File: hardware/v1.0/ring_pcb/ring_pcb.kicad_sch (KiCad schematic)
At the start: 14 parts

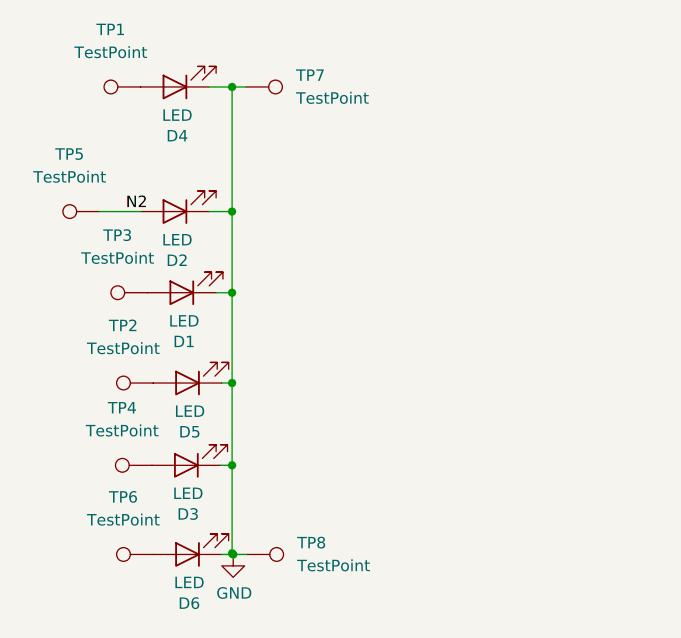
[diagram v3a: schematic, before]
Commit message: More vias and keepouts
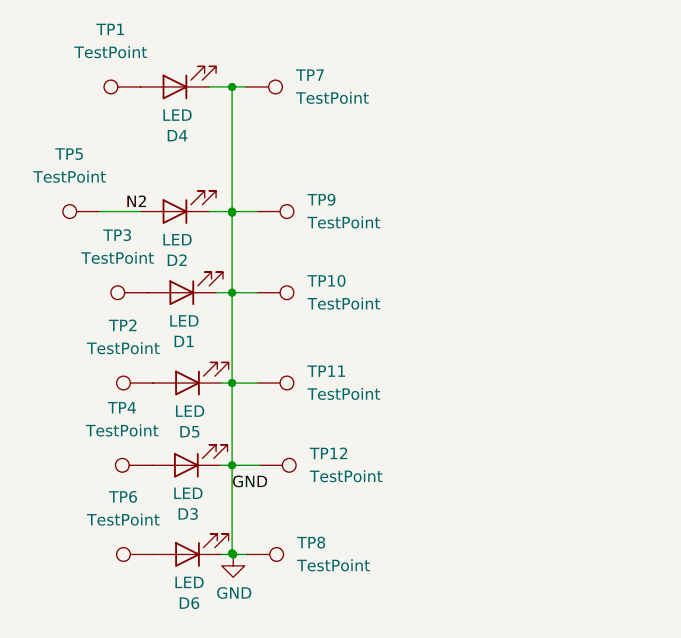
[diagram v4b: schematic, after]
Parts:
- added TP10, TP11, TP12, TP9: TestPoint, TestPoint:TestPoint_Pad_1.5x1.5mm, symbol Connector:TestPoint
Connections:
- net GND: now also D1.1 (K), D2.1 (K), D3.1 (K), D4.1 (K), D5.1 (K), TP7.1, TP10.1, TP11.1, TP12.1, TP9.1
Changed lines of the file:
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@@
 (kicad_sch (version 20210621) (generator eeschema)
   (paper "A4")
+  (junction (at 127.508 116.713) (diameter 0) (color 0 0 0 0))
+  (junction (at 127.508 87.757) (diameter 0) (color 0 0 0 0))
   (junction (at 127.508 106.934) (diameter 0) (color 0 0 0 0))
-  (junction (at 127.508 116.713) (diameter 0) (color 0 0 0 0))
-  (junction (at 127.635 116.84) (diameter 0) (color 0 0 0 0))
-  (junction (at 127.508 87.757) (diameter 0) (color 0 0 0 0))
-  (junction (at 127.508 97.79) (diameter 0) (color 0 0 0 0))
   (junction (at 127.508 78.74) (diameter 0) (color 0 0 0 0))
   (junction (at 127.508 64.897) (diameter 0) (color 0 0 0 0))
+  (junction (at 127.508 78.867) (diameter 0) (color 0 0 0 0))
+  (junction (at 127.508 97.79) (diameter 0) (color 0 0 0 0))
+  (junction (at 127.635 116.84) (diameter 0) (color 0 0 0 0))
+  (wire (pts (xy 130.302 78.74) (xy 127.508 78.74))
+    (stroke (width 0) (type default) (color 0 0 0 0))
+  )
+  (wire (pts (xy 127.508 87.757) (xy 130.302 87.757))
+    (stroke (width 0) (type default) (color 0 0 0 0))
+  )
+  (wire (pts (xy 130.556 106.934) (xy 127.508 106.934))
+    (stroke (width 0) (type default) (color 0 0 0 0))
+  )
   (wire (pts (xy 112.776 78.74) (xy 117.348 78.74))
     (stroke (width 0) (type default) (color 0 0 0 0))
   )
+  (wire (pts (xy 127.508 97.79) (xy 130.302 97.79))
+    (stroke (width 0) (type default) (color 0 0 0 0))
+  )
   (wire (pts (xy 126.365 97.79) (xy 127.508 97.79))
     (stroke (width 0) (type default) (color 0 0 0 0))
   )
+  (wire (pts (xy 127.508 78.867) (xy 127.508 78.74))
+    (stroke (width 0) (type default) (color 0 0 0 0))
+  )
+  (wire (pts (xy 127.508 64.897) (xy 127.508 64.77))
+    (stroke (width 0) (type default) (color 0 0 0 0))
+  )
+  (wire (pts (xy 127.508 78.74) (xy 127.508 64.897))
+    (stroke (width 0) (type default) (color 0 0 0 0))
+  )
+  (wire (pts (xy 127.508 87.757) (xy 127.508 78.867))
+    (stroke (width 0) (type default) (color 0 0 0 0))
+  )
   (wire (pts (xy 127.508 106.934) (xy 127.508 97.79))
     (stroke (width 0) (type default) (color 0 0 0 0))
   )
-  (wire (pts (xy 127.508 116.713) (xy 127.508 106.934))
-    (stroke (width 0) (type default) (color 0 0 0 0))
-  )
-  (wire (pts (xy 127.508 64.897) (xy 127.508 64.77))
+  (wire (pts (xy 127.508 106.934) (xy 127.508 116.713))
     (stroke (width 0) (type default) (color 0 0 0 0))
   )
@@
     (stroke (width 0) (type default) (color 0 0 0 0))
   )
-  (wire (pts (xy 127.508 78.74) (xy 127.508 64.897))
-    (stroke (width 0) (type default) (color 0 0 0 0))
-  )
-  (wire (pts (xy 127.508 87.757) (xy 127.508 78.74))
-    (stroke (width 0) (type default) (color 0 0 0 0))
-  )
   (wire (pts (xy 129.032 64.897) (xy 127.508 64.897))
     (stroke (width 0) (type default) (color 0 0 0 0))
@@
     (stroke (width 0) (type default) (color 0 0 0 0))
   )
+  (wire (pts (xy 127.635 116.84) (xy 126.365 116.84))
+    (stroke (width 0) (type default) (color 0 0 0 0))
+  )
   (wire (pts (xy 129.159 116.84) (xy 127.635 116.84))
     (stroke (width 0) (type default) (color 0 0 0 0))
   )
-  (wire (pts (xy 127.635 116.84) (xy 126.365 116.84))
-    (stroke (width 0) (type default) (color 0 0 0 0))
-  )
   (wire (pts (xy 126.238 106.934) (xy 127.508 106.934))
     (stroke (width 0) (type default) (color 0 0 0 0))
@@
   (wire (pts (xy 125.73 87.757) (xy 127.508 87.757))
     (stroke (width 0) (type default) (color 0 0 0 0))
+  )
+  (label "GND" (at 127.508 109.855 0)
+    (effects (font (size 1.27 1.27)) (justify left bottom))
   )
   (label "N2" (at 115.697 78.74 0)
@@
     (pin "2")
   )
+  (symbol (lib_id "Connector:TestPoint") (at 130.556 106.934 270) (unit 1)
+    (in_bom yes) (on_board yes) (fields_autoplaced)
+    (property "Reference" "TP12" (id 0) (at 136.144 105.6639 90)
+      (effects (font (size 1.27 1.27)) (justify left))
+    )
+    (property "Value" "TestPoint" (id 1) (at 136.144 108.2039 90)
+      (effects (font (size 1.27 1.27)) (justify left))
+    )
+    (property "Footprint" "TestPoint:TestPoint_Pad_1.5x1.5mm" (id 2) (at 130.556 112.014 0)
+      (effects (font (size 1.27 1.27)) hide)
+    )
+    (property "Datasheet" "~" (id 3) (at 130.556 112.014 0)
+      (effects (font (size 1.27 1.27)) hide)
+    )
+    (pin "1")
+  )
   (symbol (lib_id "Connector:TestPoint") (at 118.745 116.84 90) (unit 1)
     (in_bom yes) (on_board yes) (fields_autoplaced)
@@
     (pin "1")
   )
+  (symbol (lib_id "Connector:TestPoint") (at 130.302 78.74 270) (unit 1)
+    (in_bom yes) (on_board yes) (fields_autoplaced)
+    (property "Reference" "TP9" (id 0) (at 135.89 77.4699 90)
+      (effects (font (size 1.27 1.27)) (justify left))
+    )
+    (property "Value" "TestPoint" (id 1) (at 135.89 80.0099 90)
+      (effects (font (size 1.27 1.27)) (justify left))
+    )
+    (property "Footprint" "TestPoint:TestPoint_Pad_1.5x1.5mm" (id 2) (at 130.302 83.82 0)
+      (effects (font (size 1.27 1.27)) hide)
+    )
+    (property "Datasheet" "~" (id 3) (at 130.302 83.82 0)
+      (effects (font (size 1.27 1.27)) hide)
+    )
+    (pin "1")
+  )
+  (symbol (lib_id "Connector:TestPoint") (at 130.302 87.757 270) (unit 1)
+    (in_bom yes) (on_board yes) (fields_autoplaced)
+    (property "Reference" "TP10" (id 0) (at 135.89 86.4869 90)
+      (effects (font (size 1.27 1.27)) (justify left))
+    )
+    (property "Value" "TestPoint" (id 1) (at 135.89 89.0269 90)
+      (effects (font (size 1.27 1.27)) (justify left))
+    )
+    (property "Footprint" "TestPoint:TestPoint_Pad_1.5x1.5mm" (id 2) (at 130.302 92.837 0)
+      (effects (font (size 1.27 1.27)) hide)
+    )
+    (property "Datasheet" "~" (id 3) (at 130.302 92.837 0)
+      (effects (font (size 1.27 1.27)) hide)
+    )
+    (pin "1")
+  )
   (symbol (lib_id "Connector:TestPoint") (at 118.11 87.757 90) (unit 1)
     (in_bom yes) (on_board yes) (fields_autoplaced)
@@
     (pin "1")
   )
+  (symbol (lib_id "Connector:TestPoint") (at 130.302 97.79 270) (unit 1)
+    (in_bom yes) (on_board yes) (fields_autoplaced)
+    (property "Reference" "TP11" (id 0) (at 135.89 96.5199 90)
+      (effects (font (size 1.27 1.27)) (justify left))
+    )
+    (property "Value" "TestPoint" (id 1) (at 135.89 99.0599 90)
+      (effects (font (size 1.27 1.27)) (justify left))
+    )
+    (property "Footprint" "TestPoint:TestPoint_Pad_1.5x1.5mm" (id 2) (at 130.302 102.87 0)
+      (effects (font (size 1.27 1.27)) hide)
+    )
+    (property "Datasheet" "~" (id 3) (at 130.302 102.87 0)
+      (effects (font (size 1.27 1.27)) hide)
+    )
+    (pin "1")
+  )
   (symbol (lib_id "Connector:TestPoint") (at 129.159 116.84 270) (unit 1)
     (in_bom yes) (on_board yes) (fields_autoplaced)
@@
       (reference "TP8") (unit 1) (value "TestPoint") (footprint "TestPoint:TestPoint_Pad_1.5x1.5mm")
     )
-  )
+    (path "/9eb5fc74-7ee2-4483-b24f-769829d8a6c2"
+      (reference "TP9") (unit 1) (value "TestPoint") (footprint "TestPoint:TestPoint_Pad_1.5x1.5mm")
+    )
+    (path "/a72b0211-01ed-437e-8ed0-dd4a1c9ad8e3"
+      (reference "TP10") (unit 1) (value "TestPoint") (footprint "TestPoint:TestPoint_Pad_1.5x1.5mm")
+    )
+    (path "/bf1b59cd-286d-4b1f-ae75-42e14253d3af"
+      (reference "TP11") (unit 1) (value "TestPoint") (footprint "TestPoint:TestPoint_Pad_1.5x1.5mm")
+    )
+    (path "/4ef79b22-88fe-45d2-99f7-8d367793e669"
+      (reference "TP12") (unit 1) (value "TestPoint") (footprint "TestPoint:TestPoint_Pad_1.5x1.5mm")
+    )
+  )

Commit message: New PCB and Gerbers
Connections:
- net N4: now reaches D4.2 (A), TP1.1
- net N5: now reaches D5.2 (A), TP2.1
- net N3: now reaches D3.2 (A), TP4.1
- net N6: now reaches D6.2 (A), TP6.1
- net N1: now reaches D1.2 (A), TP3.1
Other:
- moved on the sheet: TP1, TP2, TP3, TP4, TP6
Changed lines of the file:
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@@
 (kicad_sch (version 20210621) (generator eeschema)
   (paper "A4")
+  (junction (at 127.508 87.757) (diameter 0) (color 0 0 0 0))
+  (junction (at 127.508 78.74) (diameter 0) (color 0 0 0 0))
   (junction (at 127.508 116.713) (diameter 0) (color 0 0 0 0))
-  (junction (at 127.508 87.757) (diameter 0) (color 0 0 0 0))
-  (junction (at 127.508 106.934) (diameter 0) (color 0 0 0 0))
-  (junction (at 127.508 78.74) (diameter 0) (color 0 0 0 0))
-  (junction (at 127.508 64.897) (diameter 0) (color 0 0 0 0))
   (junction (at 127.508 78.867) (diameter 0) (color 0 0 0 0))
   (junction (at 127.508 97.79) (diameter 0) (color 0 0 0 0))
+  (junction (at 127.508 64.897) (diameter 0) (color 0 0 0 0))
+  (junction (at 127.508 106.934) (diameter 0) (color 0 0 0 0))
   (junction (at 127.635 116.84) (diameter 0) (color 0 0 0 0))
+  (wire (pts (xy 113.792 97.79) (xy 118.745 97.79))
+    (stroke (width 0) (type default) (color 0 0 0 0))
+  )
   (wire (pts (xy 130.302 78.74) (xy 127.508 78.74))
     (stroke (width 0) (type default) (color 0 0 0 0))
@@
     (stroke (width 0) (type default) (color 0 0 0 0))
   )
+  (wire (pts (xy 114.173 116.84) (xy 118.745 116.84))
+    (stroke (width 0) (type default) (color 0 0 0 0))
+  )
   (wire (pts (xy 130.556 106.934) (xy 127.508 106.934))
     (stroke (width 0) (type default) (color 0 0 0 0))
   )
+  (wire (pts (xy 114.3 106.934) (xy 118.618 106.934))
+    (stroke (width 0) (type default) (color 0 0 0 0))
+  )
   (wire (pts (xy 112.776 78.74) (xy 117.348 78.74))
     (stroke (width 0) (type default) (color 0 0 0 0))
@@
     (stroke (width 0) (type default) (color 0 0 0 0))
   )
+  (wire (pts (xy 127.508 87.757) (xy 127.508 78.867))
+    (stroke (width 0) (type default) (color 0 0 0 0))
+  )
   (wire (pts (xy 127.508 78.867) (xy 127.508 78.74))
     (stroke (width 0) (type default) (color 0 0 0 0))
@@
     (stroke (width 0) (type default) (color 0 0 0 0))
   )
-  (wire (pts (xy 127.508 87.757) (xy 127.508 78.867))
+  (wire (pts (xy 127.508 97.79) (xy 127.508 87.757))
     (stroke (width 0) (type default) (color 0 0 0 0))
   )
@@
     (stroke (width 0) (type default) (color 0 0 0 0))
   )
-  (wire (pts (xy 127.508 97.79) (xy 127.508 87.757))
-    (stroke (width 0) (type default) (color 0 0 0 0))
-  )
   (wire (pts (xy 129.032 64.897) (xy 127.508 64.897))
     (stroke (width 0) (type default) (color 0 0 0 0))
@@
     (stroke (width 0) (type default) (color 0 0 0 0))
   )
+  (wire (pts (xy 112.776 64.897) (xy 117.348 64.897))
+    (stroke (width 0) (type default) (color 0 0 0 0))
+  )
+  (wire (pts (xy 129.159 116.84) (xy 127.635 116.84))
+    (stroke (width 0) (type default) (color 0 0 0 0))
+  )
   (wire (pts (xy 127.635 116.84) (xy 126.365 116.84))
     (stroke (width 0) (type default) (color 0 0 0 0))
   )
-  (wire (pts (xy 129.159 116.84) (xy 127.635 116.84))
-    (stroke (width 0) (type default) (color 0 0 0 0))
-  )
   (wire (pts (xy 126.238 106.934) (xy 127.508 106.934))
     (stroke (width 0) (type default) (color 0 0 0 0))
@@
     (stroke (width 0) (type default) (color 0 0 0 0))
   )
+  (wire (pts (xy 113.157 87.757) (xy 118.11 87.757))
+    (stroke (width 0) (type default) (color 0 0 0 0))
+  )
+  (label "N3" (at 115.951 106.934 0)
+    (effects (font (size 1.27 1.27)) (justify left bottom))
+  )
   (label "GND" (at 127.508 109.855 0)
     (effects (font (size 1.27 1.27)) (justify left bottom))
   )
-  (label "N2" (at 115.697 78.74 0)
+  (label "N1" (at 114.808 87.757 0)
+    (effects (font (size 1.27 1.27)) (justify left bottom))
+  )
+  (label "N5" (at 115.697 97.79 0)
+    (effects (font (size 1.27 1.27)) (justify left bottom))
+  )
+  (label "N2" (at 114.173 78.74 0)
+    (effects (font (size 1.27 1.27)) (justify left bottom))
+  )
+  (label "N4" (at 114.554 64.897 0)
+    (effects (font (size 1.27 1.27)) (justify left bottom))
+  )
+  (label "N6" (at 115.951 116.84 0)
     (effects (font (size 1.27 1.27)) (justify left bottom))
   )
@@
     (pin "2")
   )
-  (symbol (lib_id "Connector:TestPoint") (at 118.745 97.79 90) (unit 1)
-    (in_bom yes) (on_board yes) (fields_autoplaced)
-    (property "Reference" "TP2" (id 0) (at 115.443 91.44 90))
-    (property "Value" "TestPoint" (id 1) (at 115.443 93.98 90))
-    (property "Footprint" "TestPoint:TestPoint_Pad_1.5x1.5mm" (id 2) (at 118.745 92.71 0)
-      (effects (font (size 1.27 1.27)) hide)
-    )
-    (property "Datasheet" "~" (id 3) (at 118.745 92.71 0)
+  (symbol (lib_id "Connector:TestPoint") (at 113.792 97.79 90) (unit 1)
+    (in_bom yes) (on_board yes) (fields_autoplaced)
+    (property "Reference" "TP2" (id 0) (at 110.49 91.44 90))
+    (property "Value" "TestPoint" (id 1) (at 110.49 93.98 90))
+    (property "Footprint" "TestPoint:TestPoint_Pad_1.5x1.5mm" (id 2) (at 113.792 92.71 0)
+      (effects (font (size 1.27 1.27)) hide)
+    )
+    (property "Datasheet" "~" (id 3) (at 113.792 92.71 0)
       (effects (font (size 1.27 1.27)) hide)
     )
@@
     (pin "1")
   )
-  (symbol (lib_id "Connector:TestPoint") (at 118.745 116.84 90) (unit 1)
-    (in_bom yes) (on_board yes) (fields_autoplaced)
-    (property "Reference" "TP6" (id 0) (at 115.443 110.49 90))
-    (property "Value" "TestPoint" (id 1) (at 115.443 113.03 90))
-    (property "Footprint" "TestPoint:TestPoint_Pad_1.5x1.5mm" (id 2) (at 118.745 111.76 0)
-      (effects (font (size 1.27 1.27)) hide)
-    )
-    (property "Datasheet" "~" (id 3) (at 118.745 111.76 0)
+  (symbol (lib_id "Connector:TestPoint") (at 114.173 116.84 90) (unit 1)
+    (in_bom yes) (on_board yes) (fields_autoplaced)
+    (property "Reference" "TP6" (id 0) (at 110.871 110.49 90))
+    (property "Value" "TestPoint" (id 1) (at 110.871 113.03 90))
+    (property "Footprint" "TestPoint:TestPoint_Pad_1.5x1.5mm" (id 2) (at 114.173 111.76 0)
+      (effects (font (size 1.27 1.27)) hide)
+    )
+    (property "Datasheet" "~" (id 3) (at 114.173 111.76 0)
       (effects (font (size 1.27 1.27)) hide)
     )
@@
     (pin "1")
   )
-  (symbol (lib_id "Connector:TestPoint") (at 118.11 87.757 90) (unit 1)
-    (in_bom yes) (on_board yes) (fields_autoplaced)
-    (property "Reference" "TP3" (id 0) (at 114.808 81.407 90))
-    (property "Value" "TestPoint" (id 1) (at 114.808 83.947 90))
-    (property "Footprint" "TestPoint:TestPoint_Pad_1.5x1.5mm" (id 2) (at 118.11 82.677 0)
-      (effects (font (size 1.27 1.27)) hide)
-    )
-    (property "Datasheet" "~" (id 3) (at 118.11 82.677 0)
-      (effects (font (size 1.27 1.27)) hide)
-    )
-    (pin "1")
-  )
-  (symbol (lib_id "Connector:TestPoint") (at 117.348 64.897 90) (unit 1)
-    (in_bom yes) (on_board yes) (fields_autoplaced)
-    (property "Reference" "TP1" (id 0) (at 114.046 58.547 90))
-    (property "Value" "TestPoint" (id 1) (at 114.046 61.087 90))
-    (property "Footprint" "TestPoint:TestPoint_Pad_1.5x1.5mm" (id 2) (at 117.348 59.817 0)
-      (effects (font (size 1.27 1.27)) hide)
-    )
-    (property "Datasheet" "~" (id 3) (at 117.348 59.817 0)
-      (effects (font (size 1.27 1.27)) hide)
-    )
-    (pin "1")
-  )
-  (symbol (lib_id "Connector:TestPoint") (at 118.618 106.934 90) (unit 1)
-    (in_bom yes) (on_board yes) (fields_autoplaced)
-    (property "Reference" "TP4" (id 0) (at 115.316 100.584 90))
-    (property "Value" "TestPoint" (id 1) (at 115.316 103.124 90))
-    (property "Footprint" "TestPoint:TestPoint_Pad_1.5x1.5mm" (id 2) (at 118.618 101.854 0)
-      (effects (font (size 1.27 1.27)) hide)
-    )
-    (property "Datasheet" "~" (id 3) (at 118.618 101.854 0)
-      (effects (font (size 1.27 1.27)) hide)
-    )
+  (symbol (lib_id "Connector:TestPoint") (at 113.157 87.757 90) (unit 1)
+    (in_bom yes) (on_board yes) (fields_autoplaced)
+    (property "Reference" "TP3" (id 0) (at 109.855 81.407 90))
+    (property "Value" "TestPoint" (id 1) (at 109.855 83.947 90))
+    (property "Footprint" "TestPoint:TestPoint_Pad_1.5x1.5mm" (id 2) (at 113.157 82.677 0)
+      (effects (font (size 1.27 1.27)) hide)
+    )
+    (property "Datasheet" "~" (id 3) (at 113.157 82.677 0)
+      (effects (font (size 1.27 1.27)) hide)
+    )
+    (pin "1")
+  )
+  (symbol (lib_id "Connector:TestPoint") (at 112.776 64.897 90) (unit 1)
+    (in_bom yes) (on_board yes) (fields_autoplaced)
+    (property "Reference" "TP1" (id 0) (at 109.474 58.547 90))
+    (property "Value" "TestPoint" (id 1) (at 109.474 61.087 90))
+    (property "Footprint" "TestPoint:TestPoint_Pad_1.5x1.5mm" (id 2) (at 112.776 59.817 0)
+      (effects (font (size 1.27 1.27)) hide)
+    )
+    (property "Datasheet" "~" (id 3) (at 112.776 59.817 0)
+      (effects (font (size 1.27 1.27)) hide)
+    )
+    (pin "1")
+  )
+  (symbol (lib_id "Connector:TestPoint") (at 114.3 106.934 90) (unit 1)
+    (in_bom yes) (on_board yes) (fields_autoplaced)
+    (property "Reference" "TP4" (id 0) (at 110.998 100.584 90))
+    (property "Value" "TestPoint" (id 1) (at 110.998 103.124 90))
+    (property "Footprint" "TestPoint:TestPoint_Pad_1.5x1.5mm" (id 2) (at 114.3 101.854 0)
+      (effects (font (size 1.27 1.27)) hide)
+    )
+    (property "Datasheet" "~" (id 3) (at 114.3 101.854 0)
+      (effects (font (size 1.27 1.27)) hide)
+    )
